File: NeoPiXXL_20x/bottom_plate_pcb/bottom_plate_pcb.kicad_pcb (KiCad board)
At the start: 2 copper layers, 94 x 94 mm, 11 parts, among them J1 Leg, J2 Leg, J3 Leg, J4 Leg

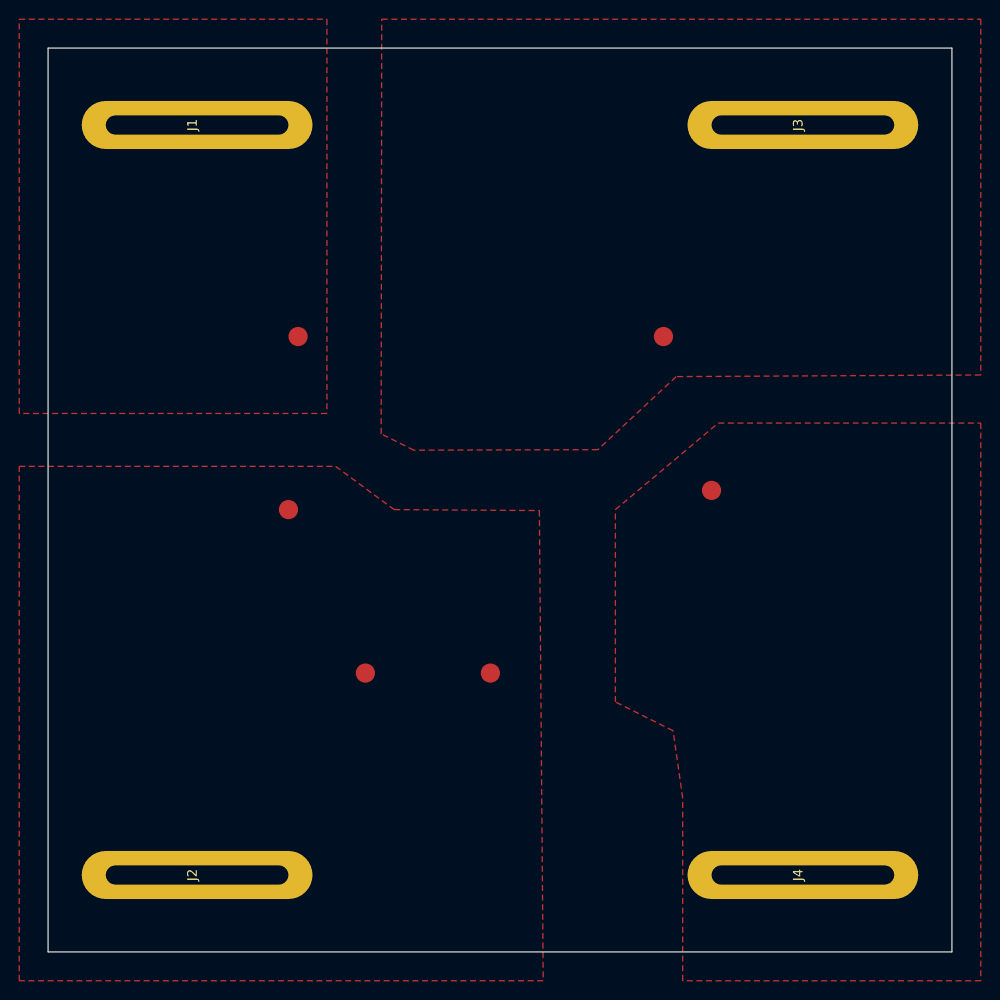
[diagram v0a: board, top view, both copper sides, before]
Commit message: add mounting holes to bottom plate
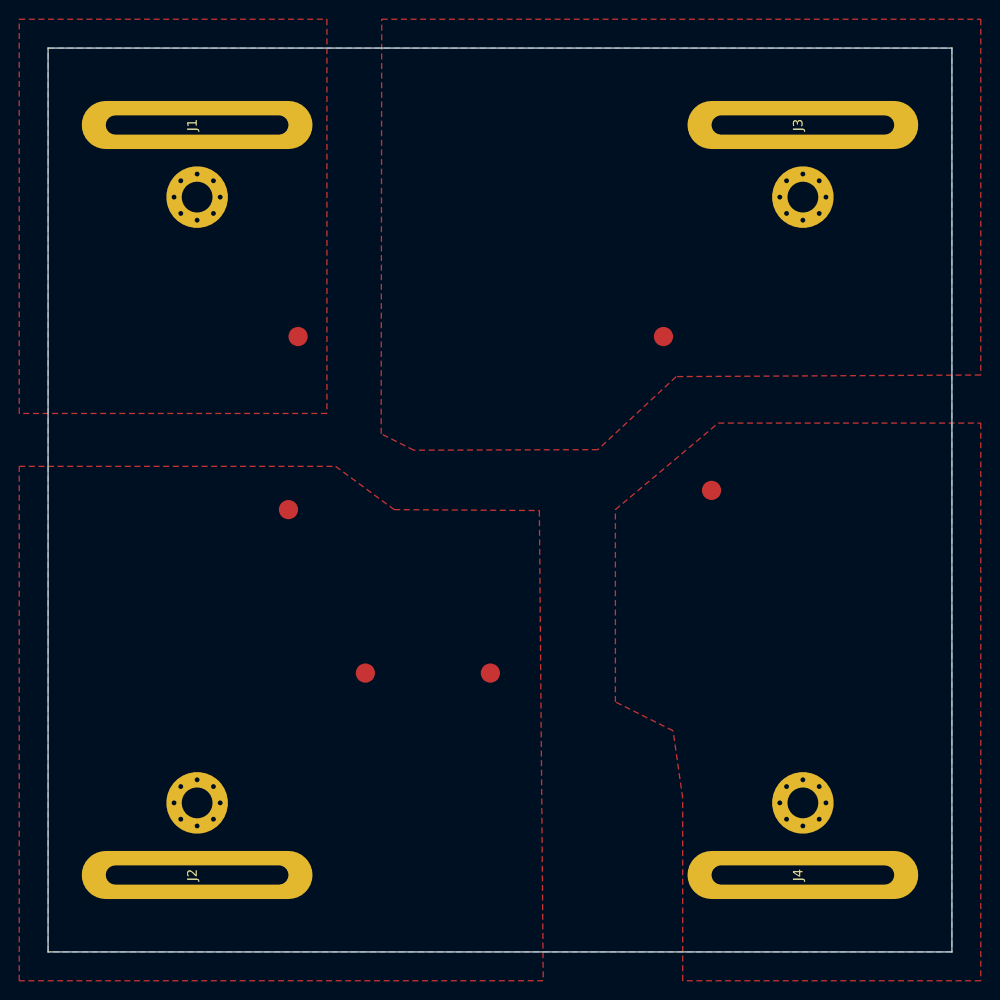
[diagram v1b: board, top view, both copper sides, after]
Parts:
- added REF**: MountingHole_3.2mm_M3_Pad_Via, MountingHole:MountingHole_3.2mm_M3_Pad_Via, F.Cu at (98.5, 130.5)
- added REF**: MountingHole_3.2mm_M3_Pad_Via, MountingHole:MountingHole_3.2mm_M3_Pad_Via, F.Cu at (161.5, 130.5)
- added REF**: MountingHole_3.2mm_M3_Pad_Via, MountingHole:MountingHole_3.2mm_M3_Pad_Via, F.Cu at (161.5, 67.5)
- added REF**: MountingHole_3.2mm_M3_Pad_Via, MountingHole:MountingHole_3.2mm_M3_Pad_Via, F.Cu at (98.5, 67.5)
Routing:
- added copper zone on B.Cu, net GND

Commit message: fixed DOUT/DIN swap for 20x variant
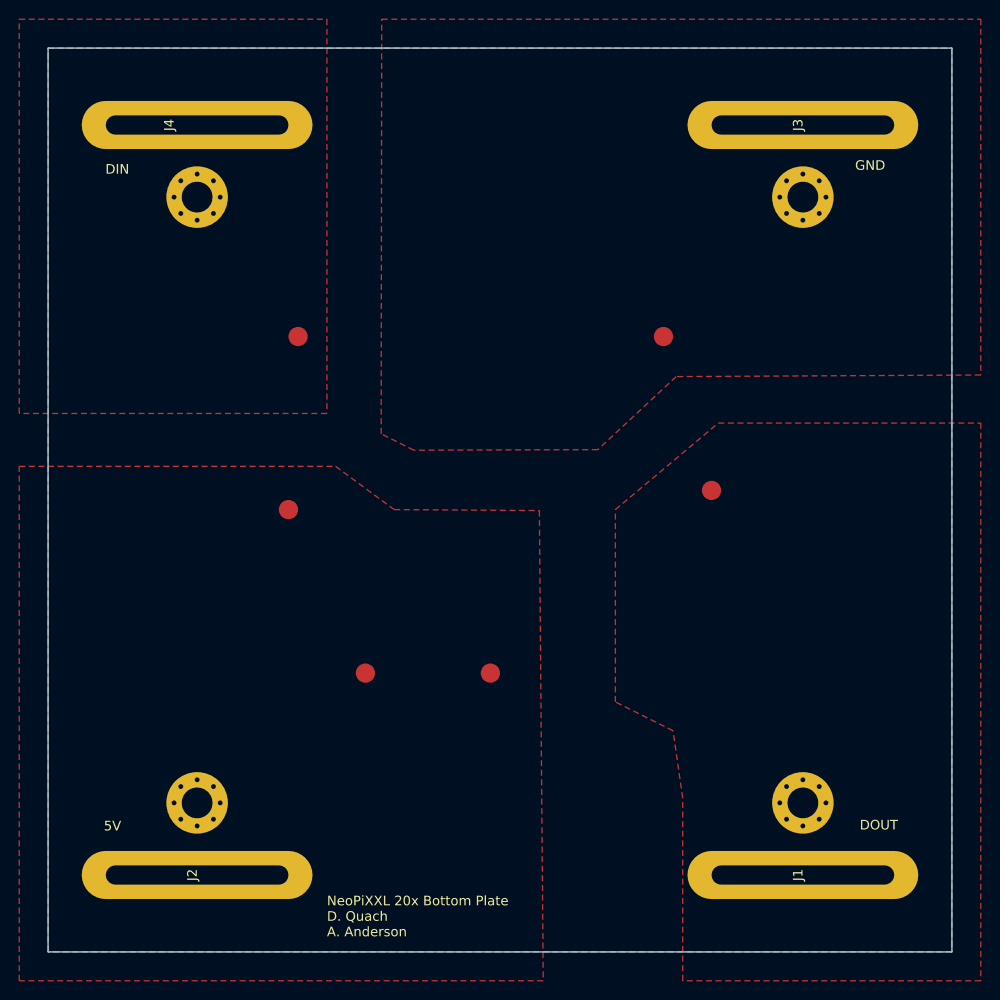
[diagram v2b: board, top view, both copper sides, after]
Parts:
- moved J1 100.3 mm to (161.5, 138.0)
- moved J4 100.3 mm to (98.5, 60.0)
- moved TP4 45.9 mm to (152.0, 98.0)
- moved TP5 45.9 mm to (109.0, 82.0)
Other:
- board text added: "5V"
- board text added: "DIN"
- board text added: "DOUT"
- board text added: "GND"
- board text added: "NeoPiXXL 20x Bottom Plate D. Quach A. Anderson"
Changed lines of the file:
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@@
       (outputformat 1)
       (mirror false)
-      (drillshape 1)
+      (drillshape 0)
       (scaleselection 1)
-      (outputdirectory "")
+      (outputdirectory "gerber_bplate/")
     )
   )
@@
   (net 4 "DIN")
   (footprint "prints:WirePad" (layer "F.Cu")
-    (at 109 82)
+    (at 152 98)
     (property "Sheetfile" "bottom_plate_pcb.kicad_sch")
     (property "Sheetname" "")
@@
   )
   (footprint "prints:pin_pad" (layer "F.Cu")
-    (at 161.5 138 90)
+    (at 98.5 60 90)
     (property "Sheetfile" "bottom_plate_pcb.kicad_sch")
     (property "Sheetname" "")
     (attr through_hole)
-    (fp_text reference "J4" (at 0 -0.5 90 unlocked) (layer "F.SilkS")
+    (fp_text reference "J4" (at 0 -2.9 90 unlocked) (layer "F.SilkS")
       (effects (font (size 1 1) (thickness 0.15)))
     )
@@
     (fp_circle (center 0 0) (end 3.2 0) (layer "Cmts.User") (width 0.15) (fill none))
     (fp_circle (center 0 0) (end 3.45 0) (layer "F.CrtYd") (width 0.05) (fill none))
+    (pad "1" thru_hole circle (at -1.697056 1.697056) (size 0.8 0.8) (drill 0.5) (layers *.Cu *.Mask))
+    (pad "1" thru_hole circle (at 0 2.4) (size 0.8 0.8) (drill 0.5) (layers *.Cu *.Mask))
+    (pad "1" thru_hole circle (at -1.697056 -1.697056) (size 0.8 0.8) (drill 0.5) (layers *.Cu *.Mask))
+    (pad "1" thru_hole circle (at 2.4 0) (size 0.8 0.8) (drill 0.5) (layers *.Cu *.Mask))
+    (pad "1" thru_hole circle (at 1.697056 -1.697056) (size 0.8 0.8) (drill 0.5) (layers *.Cu *.Mask))
+    (pad "1" thru_hole circle (at -2.4 0) (size 0.8 0.8) (drill 0.5) (layers *.Cu *.Mask))
+    (pad "1" thru_hole circle (at 1.697056 1.697056) (size 0.8 0.8) (drill 0.5) (layers *.Cu *.Mask))
+    (pad "1" thru_hole circle (at 0 0) (size 6.4 6.4) (drill 3.2) (layers *.Cu *.Mask))
     (pad "1" thru_hole circle (at 0 -2.4) (size 0.8 0.8) (drill 0.5) (layers *.Cu *.Mask))
-    (pad "1" thru_hole circle (at -2.4 0) (size 0.8 0.8) (drill 0.5) (layers *.Cu *.Mask))
-    (pad "1" thru_hole circle (at -1.697056 1.697056) (size 0.8 0.8) (drill 0.5) (layers *.Cu *.Mask))
-    (pad "1" thru_hole circle (at -1.697056 -1.697056) (size 0.8 0.8) (drill 0.5) (layers *.Cu *.Mask))
-    (pad "1" thru_hole circle (at 0 2.4) (size 0.8 0.8) (drill 0.5) (layers *.Cu *.Mask))
-    (pad "1" thru_hole circle (at 2.4 0) (size 0.8 0.8) (drill 0.5) (layers *.Cu *.Mask))
-    (pad "1" thru_hole circle (at 1.697056 1.697056) (size 0.8 0.8) (drill 0.5) (layers *.Cu *.Mask))
-    (pad "1" thru_hole circle (at 1.697056 -1.697056) (size 0.8 0.8) (drill 0.5) (layers *.Cu *.Mask))
-    (pad "1" thru_hole circle (at 0 0) (size 6.4 6.4) (drill 3.2) (layers *.Cu *.Mask))
   )
   (footprint "prints:WirePad" (layer "F.Cu")
@@
     (fp_circle (center 0 0) (end 3.2 0) (layer "Cmts.User") (width 0.15) (fill none))
     (fp_circle (center 0 0) (end 3.45 0) (layer "F.CrtYd") (width 0.05) (fill none))
+    (pad "1" thru_hole circle (at 0 2.4) (size 0.8 0.8) (drill 0.5) (layers *.Cu *.Mask))
+    (pad "1" thru_hole circle (at -1.697056 1.697056) (size 0.8 0.8) (drill 0.5) (layers *.Cu *.Mask))
+    (pad "1" thru_hole circle (at 1.697056 1.697056) (size 0.8 0.8) (drill 0.5) (layers *.Cu *.Mask))
     (pad "1" thru_hole circle (at 0 -2.4) (size 0.8 0.8) (drill 0.5) (layers *.Cu *.Mask))
+    (pad "1" thru_hole circle (at 0 0) (size 6.4 6.4) (drill 3.2) (layers *.Cu *.Mask))
+    (pad "1" thru_hole circle (at -1.697056 -1.697056) (size 0.8 0.8) (drill 0.5) (layers *.Cu *.Mask))
+    (pad "1" thru_hole circle (at 1.697056 -1.697056) (size 0.8 0.8) (drill 0.5) (layers *.Cu *.Mask))
+    (pad "1" thru_hole circle (at 2.4 0) (size 0.8 0.8) (drill 0.5) (layers *.Cu *.Mask))
     (pad "1" thru_hole circle (at -2.4 0) (size 0.8 0.8) (drill 0.5) (layers *.Cu *.Mask))
-    (pad "1" thru_hole circle (at -1.697056 1.697056) (size 0.8 0.8) (drill 0.5) (layers *.Cu *.Mask))
-    (pad "1" thru_hole circle (at -1.697056 -1.697056) (size 0.8 0.8) (drill 0.5) (layers *.Cu *.Mask))
-    (pad "1" thru_hole circle (at 0 2.4) (size 0.8 0.8) (drill 0.5) (layers *.Cu *.Mask))
-    (pad "1" thru_hole circle (at 2.4 0) (size 0.8 0.8) (drill 0.5) (layers *.Cu *.Mask))
-    (pad "1" thru_hole circle (at 1.697056 1.697056) (size 0.8 0.8) (drill 0.5) (layers *.Cu *.Mask))
-    (pad "1" thru_hole circle (at 1.697056 -1.697056) (size 0.8 0.8) (drill 0.5) (layers *.Cu *.Mask))
-    (pad "1" thru_hole circle (at 0 0) (size 6.4 6.4) (drill 3.2) (layers *.Cu *.Mask))
   )
   (footprint "prints:pin_pad" (layer "F.Cu")
@@
     (fp_circle (center 0 0) (end 3.2 0) (layer "Cmts.User") (width 0.15) (fill none))
     (fp_circle (center 0 0) (end 3.45 0) (layer "F.CrtYd") (width 0.05) (fill none))
-    (pad "1" thru_hole circle (at 0 -2.4) (size 0.8 0.8) (drill 0.5) (layers *.Cu *.Mask))
+    (pad "1" thru_hole circle (at 0 0) (size 6.4 6.4) (drill 3.2) (layers *.Cu *.Mask))
+    (pad "1" thru_hole circle (at 1.697056 -1.697056) (size 0.8 0.8) (drill 0.5) (layers *.Cu *.Mask))
+    (pad "1" thru_hole circle (at 0 2.4) (size 0.8 0.8) (drill 0.5) (layers *.Cu *.Mask))
     (pad "1" thru_hole circle (at -2.4 0) (size 0.8 0.8) (drill 0.5) (layers *.Cu *.Mask))
-    (pad "1" thru_hole circle (at -1.697056 1.697056) (size 0.8 0.8) (drill 0.5) (layers *.Cu *.Mask))
-    (pad "1" thru_hole circle (at -1.697056 -1.697056) (size 0.8 0.8) (drill 0.5) (layers *.Cu *.Mask))
-    (pad "1" thru_hole circle (at 0 2.4) (size 0.8 0.8) (drill 0.5) (layers *.Cu *.Mask))
     (pad "1" thru_hole circle (at 2.4 0) (size 0.8 0.8) (drill 0.5) (layers *.Cu *.Mask))
     (pad "1" thru_hole circle (at 1.697056 1.697056) (size 0.8 0.8) (drill 0.5) (layers *.Cu *.Mask))
-    (pad "1" thru_hole circle (at 1.697056 -1.697056) (size 0.8 0.8) (drill 0.5) (layers *.Cu *.Mask))
-    (pad "1" thru_hole circle (at 0 0) (size 6.4 6.4) (drill 3.2) (layers *.Cu *.Mask))
+    (pad "1" thru_hole circle (at -1.697056 -1.697056) (size 0.8 0.8) (drill 0.5) (layers *.Cu *.Mask))
+    (pad "1" thru_hole circle (at 0 -2.4) (size 0.8 0.8) (drill 0.5) (layers *.Cu *.Mask))
+    (pad "1" thru_hole circle (at -1.697056 1.697056) (size 0.8 0.8) (drill 0.5) (layers *.Cu *.Mask))
   )
   (footprint "prints:pin_pad" (layer "F.Cu")
@@
   )
   (footprint "prints:pin_pad" (layer "F.Cu")
-    (at 98.5 60 90)
+    (at 161.5 138 90)
     (property "Sheetfile" "bottom_plate_pcb.kicad_sch")
     (property "Sheetname" "")
@@
   )
   (footprint "prints:WirePad" (layer "F.Cu")
-    (at 152 98)
+    (at 109 82)
     (property "Sheetfile" "bottom_plate_pcb.kicad_sch")
     (property "Sheetname" "")
@@
   (gr_line (start 180 49) (end 80 149) (layer "F.Fab") (width 0.1))
   (gr_line (start 80 49) (end 180 149) (layer "F.Fab") (width 0.1))
-  (zone (net 4) (net_name "DIN") (layer "F.Cu") (hatch edge 0.508)
+  (gr_text "NeoPiXXL 20x Bottom Plate\nD. Quach\nA. Anderson" (at 112 142.3) (layer "F.SilkS")
+    (effects (font (size 1 1) (thickness 0.15)) (justify left))
+  )
+  (gr_text "DOUT" (at 169.4 132.8) (layer "F.SilkS")
+    (effects (font (size 1 1) (thickness 0.15)))
+  )
+  (gr_text "5V" (at 89.7 132.9) (layer "F.SilkS")
+    (effects (font (size 1 1) (thickness 0.15)))
+  )
+  (gr_text "GND\n" (at 168.5 64.2) (layer "F.SilkS")
+    (effects (font (size 1 1) (thickness 0.15)))
+  )
+  (gr_text "DIN" (at 90.2 64.6) (layer "F.SilkS")
+    (effects (font (size 1 1) (thickness 0.15)))
+  )
+  (zone (net 1) (net_name "DOUT") (layer "F.Cu") (hatch edge 0.508)
     (connect_pads (clearance 0.508))
     (min_thickness 0.254) (filled_areas_thickness no)
@@
     )
   )
-  (zone (net 1) (net_name "DOUT") (layer "F.Cu") (hatch edge 0.508)
+  (zone (net 4) (net_name "DIN") (layer "F.Cu") (hatch edge 0.508)
     (connect_pads (clearance 0.508))
     (min_thickness 0.254) (filled_areas_thickness no)
